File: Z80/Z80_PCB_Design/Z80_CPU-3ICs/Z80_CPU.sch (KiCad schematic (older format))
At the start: 47 parts, among them J1 USB_B, J2 Conn_01x12, J3 Conn_01x12, J4 Conn_01x02, U1 Z80CPU, U2 AS6C4008, U3 4.9152 MHz, U4 CY8C5267AXI-LP051, U5 MCP23017_SP, Y1 32.768KHz

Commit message: pls
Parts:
- C16: value 0.01uF -> 0.001uF
- C7, C8: value 10pF -> 8pF
- U2: footprint (none) -> Package_DIP:DIP-32_W15.24mm
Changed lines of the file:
@@
 F 0 "D1" V 8996 3632 50  0000 R CNN
 F 1 "LED" V 8905 3632 50  0000 R CNN
-F 2 "LED_THT:LED_D3.0mm_Horizontal_O1.27mm_Z2.0mm" V 8950 3700 50  0001 C CNN
+F 2 "LED_THT:LED_D3.0mm_Horizontal_O1.27mm_Z2.0mm" H 8950 3900 30  0000 C CNN
 F 3 "~" V 8950 3700 50  0001 C CNN
 	1    8950 3700
@@
 F 0 "R7" H 9020 4046 50  0000 L CNN
 F 1 "330" H 9020 3955 50  0000 L CNN
-F 2 "Resistor_SMD:R_0805_2012Metric_Pad1.15x1.40mm_HandSolder" V 8880 4000 50  0001 C CNN
+F 2 "Resistor_SMD:R_0805_2012Metric_Pad1.15x1.40mm_HandSolder" V 8700 4000 30  0000 C CNN
 F 3 "~" H 8950 4000 50  0001 C CNN
 	1    8950 4000
@@
 P 14100 6150
 F 0 "C7" H 14215 6196 50  0000 L CNN
-F 1 "10pF" H 14215 6105 50  0000 L CNN
+F 1 "8pF" H 14215 6105 50  0000 L CNN
 F 2 "Capacitor_SMD:C_0805_2012Metric_Pad1.15x1.40mm_HandSolder" H 14138 6000 50  0001 C CNN
 F 3 "~" H 14100 6150 50  0001 C CNN
@@
 P 14100 6550
 F 0 "C8" H 14215 6596 50  0000 L CNN
-F 1 "10pF" H 14215 6505 50  0000 L CNN
+F 1 "8pF" H 14215 6505 50  0000 L CNN
 F 2 "Capacitor_SMD:C_0805_2012Metric_Pad1.15x1.40mm_HandSolder" H 14138 6400 50  0001 C CNN
 F 3 "~" H 14100 6550 50  0001 C CNN
@@
 F 0 "BT1" V 11000 1900 50  0000 R CNN
 F 1 "Battery_Cell" V 10900 1900 50  0000 R CNN
-F 2 "Battery:BatteryHolder_Keystone_103_1x20mm" V 10950 1960 50  0001 C CNN
+F 2 "Battery:BatteryHolder_Keystone_103_1x20mm" H 10950 1000 30  0000 C CNN
 F 3 "~" V 10950 1960 50  0001 C CNN
 	1    10950 1900
@@
 F 0 "H2" H 8500 4550 50  0000 C CNN
 F 1 "Conn_01x04" H 8500 5050 50  0000 C CNN
-F 2 "Connector_PinHeader_2.54mm:PinHeader_1x04_P2.54mm_Vertical" H 8500 4850 50  0001 C CNN
+F 2 "Connector_PinHeader_2.54mm:PinHeader_1x04_P2.54mm_Vertical" H 8500 5100 30  0000 C CNN
 F 3 "~" H 8500 4850 50  0001 C CNN
 	1    8500 4850
@@
 F 0 "C3" V 11600 1500 50  0000 C CNN
 F 1 "1uF" V 11500 1500 50  0000 C CNN
-F 2 "Capacitor_SMD:C_0805_2012Metric_Pad1.15x1.40mm_HandSolder" H 11550 1600 50  0001 C CNN
+F 2 "Capacitor_SMD:C_0805_2012Metric_Pad1.15x1.40mm_HandSolder" H 11550 1200 30  0000 C CNN
 F 3 "~" H 11550 1600 50  0001 C CNN
 	1    11550 1600
@@
 F 0 "C5" V 12000 1500 50  0000 C CNN
 F 1 "1uF" V 11900 1500 50  0000 C CNN
-F 2 "Capacitor_SMD:C_0805_2012Metric_Pad1.15x1.40mm_HandSolder" H 11950 1600 50  0001 C CNN
+F 2 "Capacitor_SMD:C_0805_2012Metric_Pad1.15x1.40mm_HandSolder" H 11950 1100 30  0000 C CNN
 F 3 "~" H 11950 1600 50  0001 C CNN
 	1    11950 1600
@@
 F 0 "C2" V 11400 1500 50  0000 C CNN
 F 1 "1uF" V 11300 1500 50  0000 C CNN
-F 2 "Capacitor_SMD:C_0805_2012Metric_Pad1.15x1.40mm_HandSolder" H 11350 1600 50  0001 C CNN
+F 2 "Capacitor_SMD:C_0805_2012Metric_Pad1.15x1.40mm_HandSolder" H 11350 1250 30  0000 C CNN
 F 3 "~" H 11350 1600 50  0001 C CNN
 	1    11350 1600
@@
 F 0 "L1" V 11200 2000 50  0000 L CNN
 F 1 "ChipInd" V 11300 1900 50  0000 L CNN
-F 2 "Inductor_SMD:L_0805_2012Metric_Pad1.15x1.40mm_HandSolder" H 11250 2050 50  0001 C CNN
+F 2 "Inductor_SMD:L_0805_2012Metric_Pad1.15x1.40mm_HandSolder" H 11250 3050 30  0000 C CNN
 F 3 "~" H 11250 2050 50  0001 C CNN
 	1    11250 2050
@@
 F 0 "C4" V 11800 1500 50  0000 C CNN
 F 1 "1uF" V 11700 1500 50  0000 C CNN
-F 2 "Capacitor_SMD:C_0805_2012Metric_Pad1.15x1.40mm_HandSolder" H 11750 1600 50  0001 C CNN
+F 2 "Capacitor_SMD:C_0805_2012Metric_Pad1.15x1.40mm_HandSolder" H 11750 1150 30  0000 C CNN
 F 3 "~" H 11750 1600 50  0001 C CNN
 	1    11750 1600
@@
 F 0 "U3" H 13700 7550 60  0000 R CNN
 F 1 "4.9152 MHz" V 13550 7450 40  0000 R CNN
-F 2 "Oscillator:Oscillator_DIP-14" H 13750 6950 60  0001 C CNN
+F 2 "Oscillator:Oscillator_DIP-14" H 13350 7000 30  0000 C CNN
 F 3 "" H 13750 6950 60  0000 C CNN
 	1    13750 7300
@@
 F 0 "U4" H 12100 7950 50  0000 C CNN
 F 1 "CY8C5267AXI-LP051" H 12100 2450 50  0000 C CNN
-F 2 "Package_QFP:TQFP-100_14x14mm_P0.5mm" H 11250 5200 50  0001 C CNN
+F 2 "Package_QFP:TQFP-100_14x14mm_P0.5mm" H 12200 2300 30  0000 C CNN
 F 3 "DOCUMENTATION" H 11150 2950 50  0001 C CNN
 	1    11250 5200
@@
 F 0 "U5" H 3100 8200 50  0000 C CNN
 F 1 "MCP23017_SP" H 3200 6300 50  0000 C CNN
-F 2 "Package_DIP:DIP-28_W7.62mm" H 3050 6250 50  0001 L CNN
+F 2 "Package_DIP:DIP-28_W7.62mm" H 3050 6250 30  0000 L CNN
 F 3 "http://ww1.microchip.com/downloads/en/DeviceDoc/20001952C.pdf" H 3050 6150 50  0001 L CNN
 	1    2850 7250
@@
 F 0 "H1" H 15050 3450 50  0000 C CNN
 F 1 "Conn_01x05" H 15150 4050 50  0000 C CNN
-F 2 "Connector_PinHeader_2.54mm:PinHeader_1x05_P2.54mm_Vertical" H 15050 3750 50  0001 C CNN
+F 2 "Connector_PinHeader_2.54mm:PinHeader_1x05_P2.54mm_Vertical" H 15650 4100 30  0000 C CNN
 F 3 "~" H 15050 3750 50  0001 C CNN
 	1    15050 3750
@@
 F 0 "U2" H 6750 8550 60  0000 C CNN
 F 1 "AS6C4008" H 6800 6050 60  0000 C CNN
-F 2 "" H 6500 7300 60  0000 C CNN
+F 2 "Package_DIP:DIP-32_W15.24mm" H 6950 5950 30  0000 C CNN
 F 3 "" H 6500 7300 60  0000 C CNN
 	1    6500 7300
@@
 P 14450 4750
 F 0 "C16" H 14250 4650 50  0000 L CNN
-F 1 "0.01uF" H 14150 4850 50  0000 L CNN
+F 1 "0.001uF" H 14100 4850 50  0000 L CNN
 F 2 "Capacitor_SMD:C_0805_2012Metric_Pad1.15x1.40mm_HandSolder" H 14488 4600 50  0001 C CNN
 F 3 "~" H 14450 4750 50  0001 C CNN
@@
 F 0 "J4" H 15230 4692 50  0000 L CNN
 F 1 "Conn_01x02" H 15230 4601 50  0000 L CNN
-F 2 "Connector_PinHeader_2.54mm:PinHeader_1x02_P2.54mm_Vertical" H 15150 4700 50  0001 C CNN
+F 2 "Connector_PinHeader_2.54mm:PinHeader_1x02_P2.54mm_Vertical" H 15700 4500 30  0000 C CNN
 F 3 "~" H 15150 4700 50  0001 C CNN
 	1    15150 4700

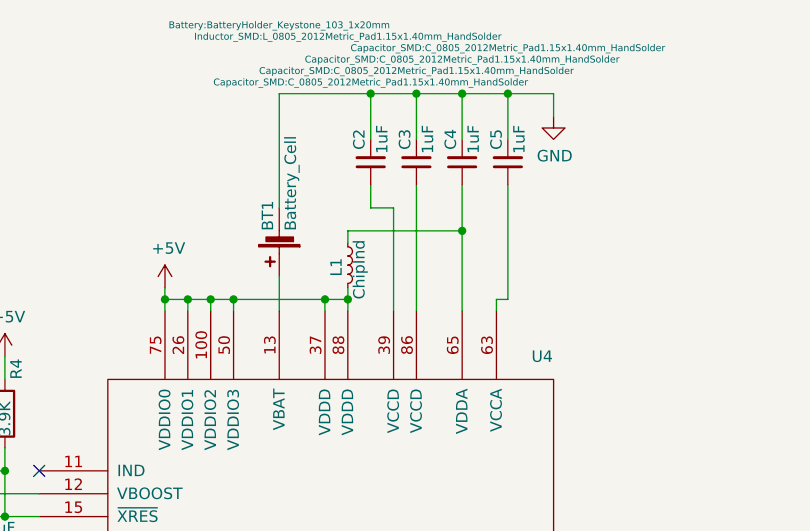
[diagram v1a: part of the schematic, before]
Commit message: Got external 512KB SRAM working
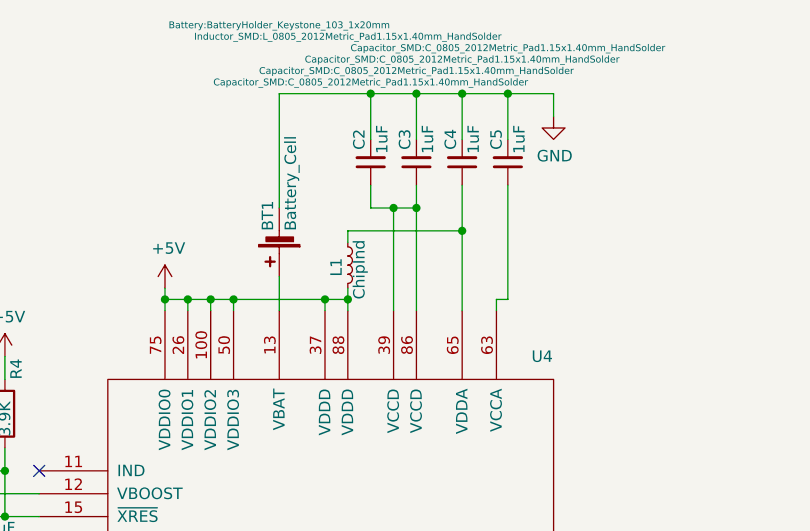
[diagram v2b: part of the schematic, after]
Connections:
- wire segments 364 -> 366
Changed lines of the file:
@@
 	11550 1300 11750 1300
 Wire Wire Line
-	11550 1700 11550 2250
+	11550 1700 11550 1800
 Wire Wire Line
 	11350 1700 11350 1800
@@
 Wire Wire Line
 	10850 9850 11150 9850
+Wire Wire Line
+	11450 1800 11550 1800
+Connection ~ 11450 1800
+Connection ~ 11550 1800
+Wire Wire Line
+	11550 1800 11550 2250
 $EndSCHEMATC

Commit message: Front panel toggle on LED release
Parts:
- renumbered C15 to C1, C2 to C10, C18 to C11, C9 to C12, C1 to C13, C11 to C14, C10 to C15, C6 to C16, C7 to C18, C8 to C19, C13 to C2, C14 to C3, C3 to C4, C17 to C5, C12 to C6, C4 to C7, C5 to C8, C16 to C9, R3 to R1, R1 to R3, R8 to R4, R9 to R5, R4 to R6, R5 to R8, R6 to R9
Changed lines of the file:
@@
 	13500 6550 13500 6500
 $Comp
-L Device:C C7
+L Device:C C18
 U 1 1 5D87A0E7
 P 14100 6150
-F 0 "C7" H 14215 6196 50  0000 L CNN
+F 0 "C18" H 14215 6196 50  0000 L CNN
 F 1 "8pF" H 14215 6105 50  0000 L CNN
 F 2 "Capacitor_SMD:C_0805_2012Metric_Pad1.15x1.40mm_HandSolder" H 14138 6000 50  0001 C CNN
@@
 $EndComp
 $Comp
-L Device:C C8
+L Device:C C19
 U 1 1 5D87A16D
 P 14100 6550
-F 0 "C8" H 14215 6596 50  0000 L CNN
+F 0 "C19" H 14215 6596 50  0000 L CNN
 F 1 "8pF" H 14215 6505 50  0000 L CNN
 F 2 "Capacitor_SMD:C_0805_2012Metric_Pad1.15x1.40mm_HandSolder" H 14138 6400 50  0001 C CNN
@@
 	9750 3150 9900 3150
 $Comp
-L Device:C_Small C1
+L Device:C_Small C13
 U 1 1 5DADD43D
 P 9550 3150
-F 0 "C1" V 9500 3050 50  0000 C CNN
+F 0 "C13" V 9400 3150 50  0000 C CNN
 F 1 "0.1uF" V 9600 3300 50  0000 C CNN
 F 2 "Capacitor_SMD:C_0805_2012Metric_Pad1.15x1.40mm_HandSolder" H 9600 2250 25  0000 C CNN
@@
 	12450 6150 12550 6150
 $Comp
-L Device:R_Small R5
+L Device:R_Small R8
 U 1 1 5DCA8222
 P 12650 6050
-F 0 "R5" V 12600 5900 50  0000 C CNN
+F 0 "R8" V 12600 5900 50  0000 C CNN
 F 1 "22" V 12750 6050 50  0000 C CNN
 F 2 "Resistor_SMD:R_0805_2012Metric_Pad1.15x1.40mm_HandSolder" H 12650 6050 50  0001 C CNN
@@
 $EndComp
 $Comp
-L Device:R_Small R6
+L Device:R_Small R9
 U 1 1 5DCA8298
 P 12650 6150
-F 0 "R6" V 12600 6000 50  0000 C CNN
+F 0 "R9" V 12600 6000 50  0000 C CNN
 F 1 "22" V 12545 6150 50  0000 C CNN
 F 2 "Resistor_SMD:R_0805_2012Metric_Pad1.15x1.40mm_HandSolder" H 12650 6150 50  0001 C CNN
@@
 	11150 2200 11250 2200
 $Comp
-L Device:C_Small C3
+L Device:C_Small C4
 U 1 1 5DEE80C9
 P 11550 1600
-F 0 "C3" V 11600 1500 50  0000 C CNN
+F 0 "C4" V 11600 1500 50  0000 C CNN
 F 1 "1uF" V 11500 1500 50  0000 C CNN
 F 2 "Capacitor_SMD:C_0805_2012Metric_Pad1.15x1.40mm_HandSolder" H 11550 1200 30  0000 C CNN
@@
 $EndComp
 $Comp
-L Device:C_Small C5
+L Device:C_Small C8
 U 1 1 5DEFFABC
 P 11950 1600
-F 0 "C5" V 12000 1500 50  0000 C CNN
+F 0 "C8" V 12000 1500 50  0000 C CNN
 F 1 "1uF" V 11900 1500 50  0000 C CNN
 F 2 "Capacitor_SMD:C_0805_2012Metric_Pad1.15x1.40mm_HandSolder" H 11950 1100 30  0000 C CNN
@@
 	11900 2200 11950 2200
 $Comp
-L Device:C_Small C2
+L Device:C_Small C10
 U 1 1 5DF17349
 P 11350 1600
-F 0 "C2" V 11400 1500 50  0000 C CNN
+F 0 "C10" V 11400 1500 50  0000 C CNN
 F 1 "1uF" V 11300 1500 50  0000 C CNN
 F 2 "Capacitor_SMD:C_0805_2012Metric_Pad1.15x1.40mm_HandSolder" H 11350 1250 30  0000 C CNN
@@
 Connection ~ 11250 2200
 $Comp
-L Device:C_Small C4
+L Device:C_Small C7
 U 1 1 5E066A76
 P 11750 1600
-F 0 "C4" V 11800 1500 50  0000 C CNN
+F 0 "C7" V 11800 1500 50  0000 C CNN
 F 1 "1uF" V 11700 1500 50  0000 C CNN
 F 2 "Capacitor_SMD:C_0805_2012Metric_Pad1.15x1.40mm_HandSolder" H 11750 1150 30  0000 C CNN
@@
 PSoC \nDownload\nConnector
 $Comp
-L Device:R R4
+L Device:R R6
 U 1 1 5EDAD430
 P 9750 2700
-F 0 "R4" V 9800 2850 50  0000 L CNN
+F 0 "R6" H 9800 2850 50  0000 L CNN
 F 1 "3.9K" V 9750 2600 50  0000 L CNN
 F 2 "Resistor_SMD:R_0805_2012Metric_Pad1.15x1.40mm_HandSolder" V 9600 3050 25  0000 C CNN
@@
 	9750 2550 9750 2450
 $Comp
-L Device:C_Small C6
+L Device:C_Small C16
 U 1 1 5F05EA7C
 P 8750 9700
-F 0 "C6" H 8650 9600 50  0000 C CNN
+F 0 "C16" H 8650 9600 50  0000 C CNN
 F 1 "0.1uF" H 8600 9800 50  0000 C CNN
 F 2 "Capacitor_SMD:C_0805_2012Metric_Pad1.15x1.40mm_HandSolder" H 8750 9900 20  0000 C CNN
@@
 	9050 9550 9350 9550
 $Comp
-L Device:C_Small C9
+L Device:C_Small C12
 U 1 1 5F78DB37
 P 9050 9700
-F 0 "C9" H 8950 9600 50  0000 C CNN
+F 0 "C12" H 8950 9600 50  0000 C CNN
 F 1 "0.1uF" H 8900 9800 50  0000 C CNN
 F 2 "Capacitor_SMD:C_0805_2012Metric_Pad1.15x1.40mm_HandSolder" H 9050 9900 20  0000 C CNN
@@
 $EndComp
 $Comp
-L Device:C_Small C10
+L Device:C_Small C15
 U 1 1 5F78DB93
 P 9350 9700
-F 0 "C10" H 9250 9600 50  0000 C CNN
+F 0 "C15" H 9250 9600 50  0000 C CNN
 F 1 "0.1uF" H 9200 9800 50  0000 C CNN
 F 2 "Capacitor_SMD:C_0805_2012Metric_Pad1.15x1.40mm_HandSolder" H 9350 9900 20  0000 C CNN
@@
 $EndComp
 $Comp
-L Device:C_Small C11
+L Device:C_Small C14
 U 1 1 5F78DBF1
 P 9650 9700
-F 0 "C11" H 9550 9600 50  0000 C CNN
+F 0 "C14" H 9550 9600 50  0000 C CNN
 F 1 "0.1uF" H 9500 9800 50  0000 C CNN
 F 2 "Capacitor_SMD:C_0805_2012Metric_Pad1.15x1.40mm_HandSolder" H 9650 9900 20  0000 C CNN
@@
 $EndComp
 $Comp
-L Device:C_Small C12
+L Device:C_Small C6
 U 1 1 5F78DC4F
 P 9950 9700
-F 0 "C12" H 9850 9600 50  0000 C CNN
+F 0 "C6" H 9850 9600 50  0000 C CNN
 F 1 "0.1uF" H 9800 9800 50  0000 C CNN
 F 2 "Capacitor_SMD:C_0805_2012Metric_Pad1.15x1.40mm_HandSolder" H 9950 9900 20  0000 C CNN
@@
 $EndComp
 $Comp
-L Device:C_Small C13
+L Device:C_Small C2
 U 1 1 5F78DCAF
 P 10250 9700
-F 0 "C13" H 10150 9600 50  0000 C CNN
+F 0 "C2" H 10150 9600 50  0000 C CNN
 F 1 "0.1uF" H 10100 9800 50  0000 C CNN
 F 2 "Capacitor_SMD:C_0805_2012Metric_Pad1.15x1.40mm_HandSolder" H 10250 9900 20  0000 C CNN
@@
 $EndComp
 $Comp
-L Device:C_Small C14
+L Device:C_Small C3
 U 1 1 5F78DD11
 P 10550 9700
-F 0 "C14" H 10450 9600 50  0000 C CNN
+F 0 "C3" H 10450 9600 50  0000 C CNN
 F 1 "0.1uF" H 10400 9800 50  0000 C CNN
 F 2 "Capacitor_SMD:C_0805_2012Metric_Pad1.15x1.40mm_HandSolder" H 10550 9900 20  0000 C CNN
@@
 $EndComp
 $Comp
-L Device:C_Small C15
+L Device:C_Small C1
 U 1 1 5F78DD79
 P 10850 9700
-F 0 "C15" H 10750 9600 50  0000 C CNN
+F 0 "C1" H 10750 9600 50  0000 C CNN
 F 1 "0.1uF" H 10700 9800 50  0000 C CNN
 F 2 "Capacitor_SMD:C_0805_2012Metric_Pad1.15x1.40mm_HandSolder" H 10850 9900 20  0000 C CNN
@@
 $EndComp
 $Comp
-L Device:C_Small C17
+L Device:C_Small C5
 U 1 1 5F78DE4B
 P 11150 9700
-F 0 "C17" H 11050 9600 50  0000 C CNN
+F 0 "C5" H 11050 9600 50  0000 C CNN
 F 1 "0.1uF" H 11000 9800 50  0000 C CNN
 F 2 "Capacitor_SMD:C_0805_2012Metric_Pad1.15x1.40mm_HandSolder" H 11150 9900 20  0000 C CNN
@@
 $EndComp
 $Comp
-L Device:C_Small C18
+L Device:C_Small C11
 U 1 1 5F78DEB9
 P 11450 9700
-F 0 "C18" H 11350 9600 50  0000 C CNN
+F 0 "C11" H 11350 9600 50  0000 C CNN
 F 1 "0.1uF" H 11300 9800 50  0000 C CNN
 F 2 "Capacitor_SMD:C_0805_2012Metric_Pad1.15x1.40mm_HandSolder" H 11450 9900 20  0000 C CNN
@@
 Connection ~ 3200 4150
 $Comp
-L Device:R R3
+L Device:R R1
 U 1 1 5D8E849B
 P 14150 3300
-F 0 "R3" H 14220 3346 50  0000 L CNN
-F 1 "2.2K" H 14220 3255 50  0000 L CNN
+F 0 "R1" H 14220 3346 50  0000 L CNN
+F 1 "2.2K" V 14150 3200 50  0000 L CNN
 F 2 "Resistor_SMD:R_0805_2012Metric_Pad1.15x1.40mm_HandSolder" V 14080 3300 50  0001 C CNN
 F 3 "~" H 14150 3300 50  0001 C CNN
@@
 P 13900 3300
 F 0 "R2" H 13970 3346 50  0000 L CNN
-F 1 "2.2K" H 13970 3255 50  0000 L CNN
+F 1 "2.2K" V 13900 3200 50  0000 L CNN
 F 2 "Resistor_SMD:R_0805_2012Metric_Pad1.15x1.40mm_HandSolder" V 13830 3300 50  0001 C CNN
 F 3 "~" H 13900 3300 50  0001 C CNN
@@
 $EndComp
 $Comp
-L Device:R R1
+L Device:R R3
 U 1 1 5D8E893F
 P 13650 3300
-F 0 "R1" H 13720 3346 50  0000 L CNN
-F 1 "2.2K" H 13720 3255 50  0000 L CNN
+F 0 "R3" H 13720 3346 50  0000 L CNN
+F 1 "2.2K" V 13650 3200 50  0000 L CNN
 F 2 "Resistor_SMD:R_0805_2012Metric_Pad1.15x1.40mm_HandSolder" V 13580 3300 50  0001 C CNN
 F 3 "~" H 13650 3300 50  0001 C CNN
@@
 	13650 3750 14850 3750
 $Comp
-L Device:R R8
+L Device:R R4
 U 1 1 5D8EA097
 P 13850 4500
-F 0 "R8" V 13750 4450 50  0000 L CNN
+F 0 "R4" V 13750 4450 50  0000 L CNN
 F 1 "2.2K" V 13950 4450 50  0000 L CNN
 F 2 "Resistor_SMD:R_0805_2012Metric_Pad1.15x1.40mm_HandSolder" V 13780 4500 50  0001 C CNN
@@
 $EndComp
 $Comp
-L Device:R R9
+L Device:R R5
 U 1 1 5D8EA175
 P 14200 4750
-F 0 "R9" H 14250 4700 50  0000 L CNN
+F 0 "R5" H 14250 4700 50  0000 L CNN
 F 1 "100" H 14250 4800 50  0000 L CNN
 F 2 "Resistor_SMD:R_0805_2012Metric_Pad1.15x1.40mm_HandSolder" V 14130 4750 50  0001 C CNN
@@
 $EndComp
 $Comp
-L Device:C C16
+L Device:C C9
 U 1 1 5D8EA2D1
 P 14450 4750
-F 0 "C16" H 14250 4650 50  0000 L CNN
+F 0 "C9" H 14250 4650 50  0000 L CNN
 F 1 "0.001uF" H 14100 4850 50  0000 L CNN
 F 2 "Capacitor_SMD:C_0805_2012Metric_Pad1.15x1.40mm_HandSolder" H 14488 4600 50  0001 C CNN
